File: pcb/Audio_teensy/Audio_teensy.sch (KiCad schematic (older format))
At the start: 20 parts, among them J1 RJ45 Jack, J2 Female Header, J3 Female Header, J4 Mono Audio Jack, J5 Mono Audio Jack, U1 Teensy3.2_smd, U2 AP7313, U3 SGTL5000

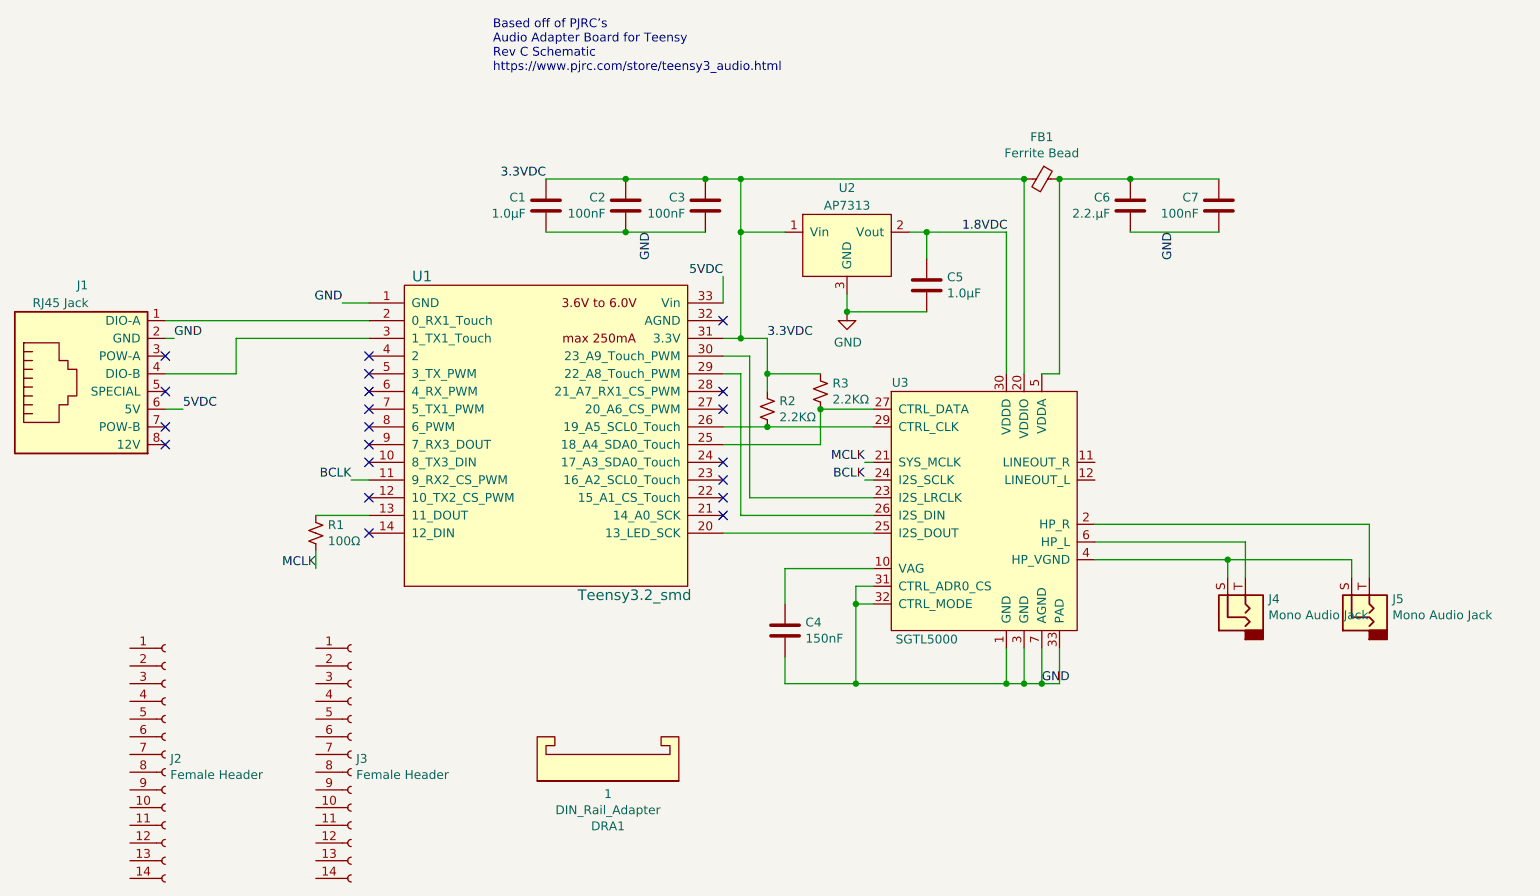
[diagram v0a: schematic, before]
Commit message: v1.1 AP3713 regulator pins were mapped incorrectly to footprint. Swapped Vin and GND. Added descriptions and purchase links for all components.
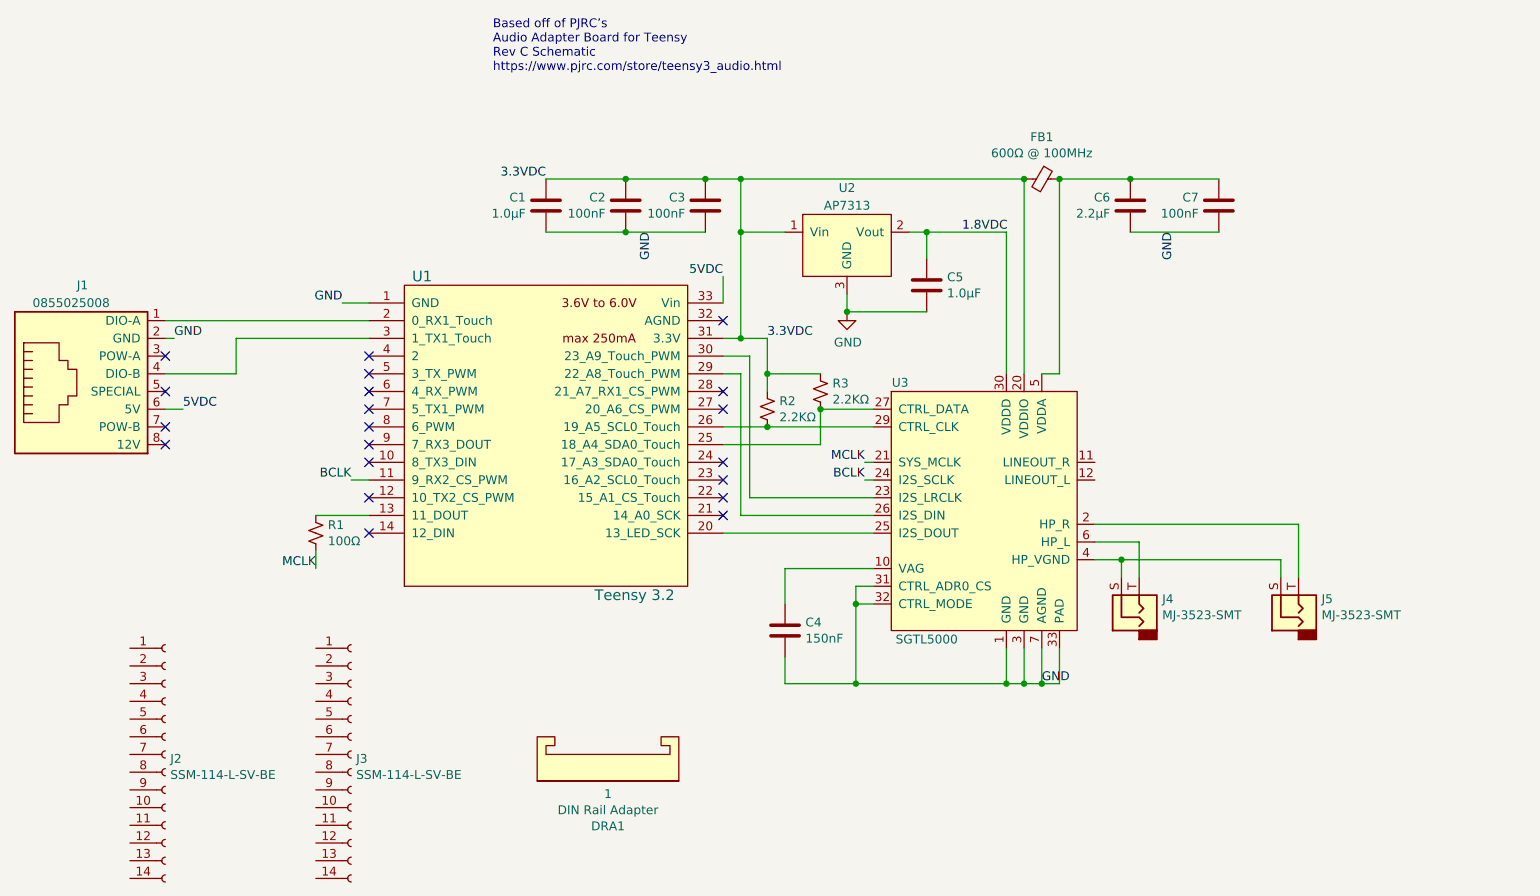
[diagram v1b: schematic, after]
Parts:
- C6: value 2.2.µF -> 2.2µF
- DRA1: value DIN_Rail_Adapter -> DIN Rail Adapter
- FB1: value Ferrite Bead -> 600Ω @ 100MHz; Description (none) -> 0603 Ferrite Bead
- J1: value RJ45 Jack -> 0855025008; Description (none) -> RJ45 Jack
- J2, J3: value Female Header -> SSM-114-L-SV-BE; Description (none) -> 14pin Female Header
- J4, J5: value Mono Audio Jack -> MJ-3523-SMT; Description (none) -> Mono Audio Jack
- U1: value Teensy3.2_smd -> Teensy 3.2
- U2: Description (none) -> 1.8V LDO Regulator
- U3: Description (none) -> Codec IC
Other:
- moved on the sheet: J4, J5
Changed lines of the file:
@@
 Sheet 1 1
 Title ""
-Date "2019-11-01"
-Rev "1.0"
+Date "2019-11-08"
+Rev "1.1"
 Comp ""
 Comment1 ""
@@
 P 2100 3500
 F 0 "J1" H 2050 2950 50  0000 L CNN
-F 1 "RJ45 Jack" H 1800 3050 50  0000 L CNN
+F 1 "0855025008" H 1800 3050 50  0000 L CNN
 F 2 "asl_footprints:RJ45_SMD" H 2150 2950 50  0001 C CNN
-F 3 "~" V 2000 3475 50  0001 C CNN
+F 3 "https://www.digikey.com/products/en?keywords=WM3547CT-ND" V 2000 3475 50  0001 C CNN
+F 4 "RJ45 Jack" H 2100 3500 50  0001 C CNN "Description"
 	1    2100 3500
 	1    0    0    1
@@
 F 2 "Package_TO_SOT_SMD:TSOT-23" H 6400 2650 50  0001 C CNN
 F 3 "https://www.digikey.com/product-detail/en/diodes-incorporated/AP7313-18SAG-7/AP7313-18SAG-7DICT-ND/2270838" H 6400 2800 50  0001 C CNN
+F 4 "1.8V LDO Regulator" H 6400 2750 50  0001 C CNN "Description"
 	1    6400 2750
 	1    0    0    -1
@@
 F 1 "1.0µF" H 6965 2905 50  0000 L CNN
 F 2 "Capacitor_SMD:C_0603_1608Metric" H 6888 2800 50  0001 C CNN
-F 3 "~" H 6850 2950 50  0001 C CNN
+F 3 "https://www.digikey.com/products/en?keywords=1276-6524-1-ND" H 6850 2950 50  0001 C CNN
+F 4 "" H 6850 2950 50  0001 C CNN "Description"
 	1    6850 2950
 	1    0    0    -1
@@
 L asl_symbols:MonoJack J4
 U 1 1 5DBB2449
-P 8650 4800
-F 0 "J4" V 8728 4670 50  0000 R CNN
-F 1 "Mono Audio Jack" V 8637 4670 50  0000 R CNN
-F 2 "asl_footprints:MonoJack" H 8650 4650 50  0001 C CNN
-F 3 "https://www.digikey.com/products/en?keywords=CP-3523MJCT-ND" H 8650 4800 50  0001 C CNN
-	1    8650 4800
+P 8050 4800
+F 0 "J4" V 8128 4670 50  0000 R CNN
+F 1 "MJ-3523-SMT" V 8037 4670 50  0000 R CNN
+F 2 "asl_footprints:MonoJack" H 8050 4650 50  0001 C CNN
+F 3 "https://www.digikey.com/products/en?keywords=CP-3523MJCT-ND" H 8050 4800 50  0001 C CNN
+F 4 "Mono Audio Jack" H 8050 4800 50  0001 C CNN "Description"
+	1    8050 4800
 	0    -1   -1   0
 $EndComp
@@
 L asl_symbols:MonoJack J5
 U 1 1 5DBB640C
-P 9350 4800
-F 0 "J5" V 9428 4670 50  0000 R CNN
-F 1 "Mono Audio Jack" V 9337 4670 50  0000 R CNN
-F 2 "asl_footprints:MonoJack" H 9350 4650 50  0001 C CNN
-F 3 "https://www.digikey.com/products/en?keywords=CP-3523MJCT-ND" H 9350 4800 50  0001 C CNN
-	1    9350 4800
+P 8950 4800
+F 0 "J5" V 9028 4670 50  0000 R CNN
+F 1 "MJ-3523-SMT" V 8937 4670 50  0000 R CNN
+F 2 "asl_footprints:MonoJack" H 8950 4650 50  0001 C CNN
+F 3 "https://www.digikey.com/products/en?keywords=CP-3523MJCT-ND" H 8950 4800 50  0001 C CNN
+F 4 "Mono Audio Jack" H 8950 4800 50  0001 C CNN "Description"
+	1    8950 4800
 	0    -1   -1   0
 $EndComp
 Wire Wire Line
-	8550 4600 8550 4500
-Wire Wire Line
-	8550 4500 7800 4500
-Wire Wire Line
-	8650 4600 8650 4400
-Wire Wire Line
-	8650 4400 7800 4400
-Wire Wire Line
-	9250 4600 9250 4500
-Wire Wire Line
-	9250 4500 8550 4500
-Connection ~ 8550 4500
-Wire Wire Line
-	9350 4600 9350 4300
-Wire Wire Line
-	9350 4300 7800 4300
+	7950 4600 7950 4500
+Wire Wire Line
+	7950 4500 7800 4500
+Wire Wire Line
+	8050 4600 8050 4400
+Wire Wire Line
+	8050 4400 7800 4400
+Wire Wire Line
+	8850 4600 8850 4500
+Wire Wire Line
+	8850 4500 7950 4500
+Connection ~ 7950 4500
+Wire Wire Line
+	8950 4600 8950 4300
+Wire Wire Line
+	8950 4300 7800 4300
 Wire Wire Line
 	3700 4050 3600 4050
@@
 F 1 "150nF" H 6165 4855 50  0000 L CNN
 F 2 "Capacitor_SMD:C_0603_1608Metric" H 6088 4750 50  0001 C CNN
-F 3 "~" H 6050 4900 50  0001 C CNN
+F 3 "https://www.digikey.com/product-detail/en/kemet/C0603C154K8RACTU/399-7862-1-ND/3471585" H 6050 4900 50  0001 C CNN
+F 4 "" H 6050 4900 50  0001 C CNN "Description"
 	1    6050 4900
 	1    0    0    -1
@@
 F 1 "100nF" H 5036 2545 50  0000 R CNN
 F 2 "Capacitor_SMD:C_0603_1608Metric" H 5188 2350 50  0001 C CNN
-F 3 "~" H 5150 2500 50  0001 C CNN
+F 3 "https://www.digikey.com/products/en?keywords=1276-1258-1-ND" H 5150 2500 50  0001 C CNN
+F 4 "" H 5150 2500 50  0001 C CNN "Description"
 	1    5150 2500
 	1    0    0    1
@@
 F 1 "100nF" H 5486 2545 50  0000 R CNN
 F 2 "Capacitor_SMD:C_0603_1608Metric" H 5638 2350 50  0001 C CNN
-F 3 "~" H 5600 2500 50  0001 C CNN
+F 3 "https://www.digikey.com/products/en?keywords=1276-1258-1-ND" H 5600 2500 50  0001 C CNN
+F 4 "" H 5600 2500 50  0001 C CNN "Description"
 	1    5600 2500
 	1    0    0    1
@@
 F 1 "1.0µF" H 4585 2545 50  0000 R CNN
 F 2 "Capacitor_SMD:C_0603_1608Metric" H 4738 2350 50  0001 C CNN
-F 3 "~" H 4700 2500 50  0001 C CNN
+F 3 "https://www.digikey.com/products/en?keywords=1276-6524-1-ND" H 4700 2500 50  0001 C CNN
+F 4 "" H 4700 2500 50  0001 C CNN "Description"
 	1    4700 2500
 	1    0    0    1
@@
 P 7500 2350
 F 0 "FB1" V 7263 2350 50  0000 C CNN
-F 1 "Ferrite Bead" V 7354 2350 50  0000 C CNN
+F 1 "600Ω @ 100MHz" V 7354 2350 50  0000 C CNN
 F 2 "Capacitor_SMD:C_0603_1608Metric" V 7430 2350 50  0001 C CNN
 F 3 "https://www.digikey.com/products/en?keywords=445-2166-1-ND" H 7500 2350 50  0001 C CNN
+F 4 "0603 Ferrite Bead" H 7500 2350 50  0001 C CNN "Description"
 	1    7500 2350
 	0    1    1    0
@@
 P 5050 5650
 F 0 "DRA1" H 5050 6005 50  0000 C CNN
-F 1 "DIN_Rail_Adapter" H 5050 5914 50  0000 C CNN
+F 1 "DIN Rail Adapter" H 5050 5914 50  0000 C CNN
 F 2 "asl_footprints:DIN_Clip" H 5050 5450 50  0001 C CNN
 F 3 "~" H 5050 5800 50  0001 C CNN
@@
 F 1 "2.2KΩ" H 6318 3505 50  0000 L CNN
 F 2 "Resistor_SMD:R_0603_1608Metric" H 6250 3550 50  0001 C CNN
-F 3 "~" H 6250 3550 50  0001 C CNN
+F 3 "https://www.digikey.com/products/en?keywords=A130093CT-ND" H 6250 3550 50  0001 C CNN
+F 4 "" H 6250 3550 50  0001 C CNN "Description"
 	1    6250 3550
 	1    0    0    -1
@@
 F 1 "2.2KΩ" H 6018 3605 50  0000 L CNN
 F 2 "Resistor_SMD:R_0603_1608Metric" H 5950 3650 50  0001 C CNN
-F 3 "~" H 5950 3650 50  0001 C CNN
+F 3 "https://www.digikey.com/products/en?keywords=A130093CT-ND" H 5950 3650 50  0001 C CNN
+F 4 "" H 5950 3650 50  0001 C CNN "Description"
 	1    5950 3650
 	1    0    0    -1
@@
 F 1 "100Ω" H 3468 4305 50  0000 L CNN
 F 2 "Resistor_SMD:R_0603_1608Metric" H 3400 4350 50  0001 C CNN
-F 3 "~" H 3400 4350 50  0001 C CNN
+F 3 "https://www.digikey.com/products/en?keywords=311-100HRCT-ND" H 3400 4350 50  0001 C CNN
+F 4 "" H 3400 4350 50  0001 C CNN "Description"
 	1    3400 4350
 	1    0    0    -1
@@
 P 8000 2500
 F 0 "C6" H 7886 2454 50  0000 R CNN
-F 1 "2.2.µF" H 7886 2545 50  0000 R CNN
+F 1 "2.2µF" H 7886 2545 50  0000 R CNN
 F 2 "Capacitor_SMD:C_0603_1608Metric" H 8038 2350 50  0001 C CNN
-F 3 "~" H 8000 2500 50  0001 C CNN
+F 3 "https://www.digikey.com/products/en?keywords=1276-1040-1-ND" H 8000 2500 50  0001 C CNN
+F 4 "" H 8000 2500 50  0001 C CNN "Description"
 	1    8000 2500
 	1    0    0    1
@@
 F 1 "100nF" H 8386 2545 50  0000 R CNN
 F 2 "Capacitor_SMD:C_0603_1608Metric" H 8538 2350 50  0001 C CNN
-F 3 "~" H 8500 2500 50  0001 C CNN
+F 3 "https://www.digikey.com/products/en?keywords=1276-1258-1-ND" H 8500 2500 50  0001 C CNN
+F 4 "" H 8500 2500 50  0001 C CNN "Description"
 	1    8500 2500
 	1    0    0    1
@@
 P 3600 5600
 F 0 "J3" H 3628 5576 50  0000 L CNN
-F 1 "Female Header" H 3628 5485 50  0000 L CNN
+F 1 "SSM-114-L-SV-BE" H 3628 5485 50  0000 L CNN
 F 2 "Connector_PinHeader_2.54mm:PinHeader_1x14_P2.54mm_Vertical_SMD_Pin1Left" H 3600 5600 50  0001 C CNN
 F 3 "https://www.digikey.com/products/en?keywords=SSM-114-L-SV-BE-ND" H 3600 5600 50  0001 C CNN
+F 4 "14pin Female Header" H 3600 5600 50  0001 C CNN "Description"
 	1    3600 5600
 	1    0    0    -1
@@
 P 2550 5600
 F 0 "J2" H 2578 5576 50  0000 L CNN
-F 1 "Female Header" H 2578 5485 50  0000 L CNN
+F 1 "SSM-114-L-SV-BE" H 2578 5485 50  0000 L CNN
 F 2 "Connector_PinHeader_2.54mm:PinHeader_1x14_P2.54mm_Vertical_SMD_Pin1Left" H 2550 5600 50  0001 C CNN
 F 3 "https://www.digikey.com/products/en?keywords=SSM-114-L-SV-BE-ND" H 2550 5600 50  0001 C CNN
+F 4 "14pin Female Header" H 2550 5600 50  0001 C CNN "Description"
 	1    2550 5600
 	1    0    0    -1
@@
 P 4700 3900
 F 0 "U1" H 4000 4900 60  0000 C CNN
-F 1 "Teensy3.2_smd" H 5200 3100 60  0000 C CNN
+F 1 "Teensy 3.2" H 5200 3100 60  0000 C CNN
 F 2 "asl_footprints:Teensy30_31_32_LC_SMD" H 4750 5050 60  0001 C CNN
 F 3 "https://www.pjrc.com/teensy/teensy31.html" H 4700 3650 60  0001 C CNN
@@
 F 2 "Package_DFN_QFN:QFN-32-1EP_5x5mm_P0.5mm_EP3.1x3.1mm" H 7200 3150 50  0001 C CNN
 F 3 "https://www.digikey.com/products/en?keywords=SGTL5000XNAA3R2CT-ND" H 6800 4250 50  0001 C CNN
+F 4 "Codec IC" H 7150 4200 50  0001 C CNN "Description"
 	1    7150 4200
 	1    0    0    -1
